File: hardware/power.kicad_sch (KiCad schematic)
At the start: 50 parts, among them J1 B2B-PH-K-S, J2 DX07S016JA1R1500, J3 PRPC001DAAN-RC, J4 PRPC001DAAN-RC, J5 PRPC001DAAN-RC, J6 PRPC001DAAN-RC, J7 PRPC001DAAN-RC, Q1 IRLML2246TRPBF, Q2 IRLML6344TRPBF, Q3 IRLML6344TRPBF, Q4 IRLML2246TRPBF, U1 USBLC6-2SC6, U2 S-8240ADQ-M6T1U, U3 BQ21040DBVR, U4 TPS63031DSK

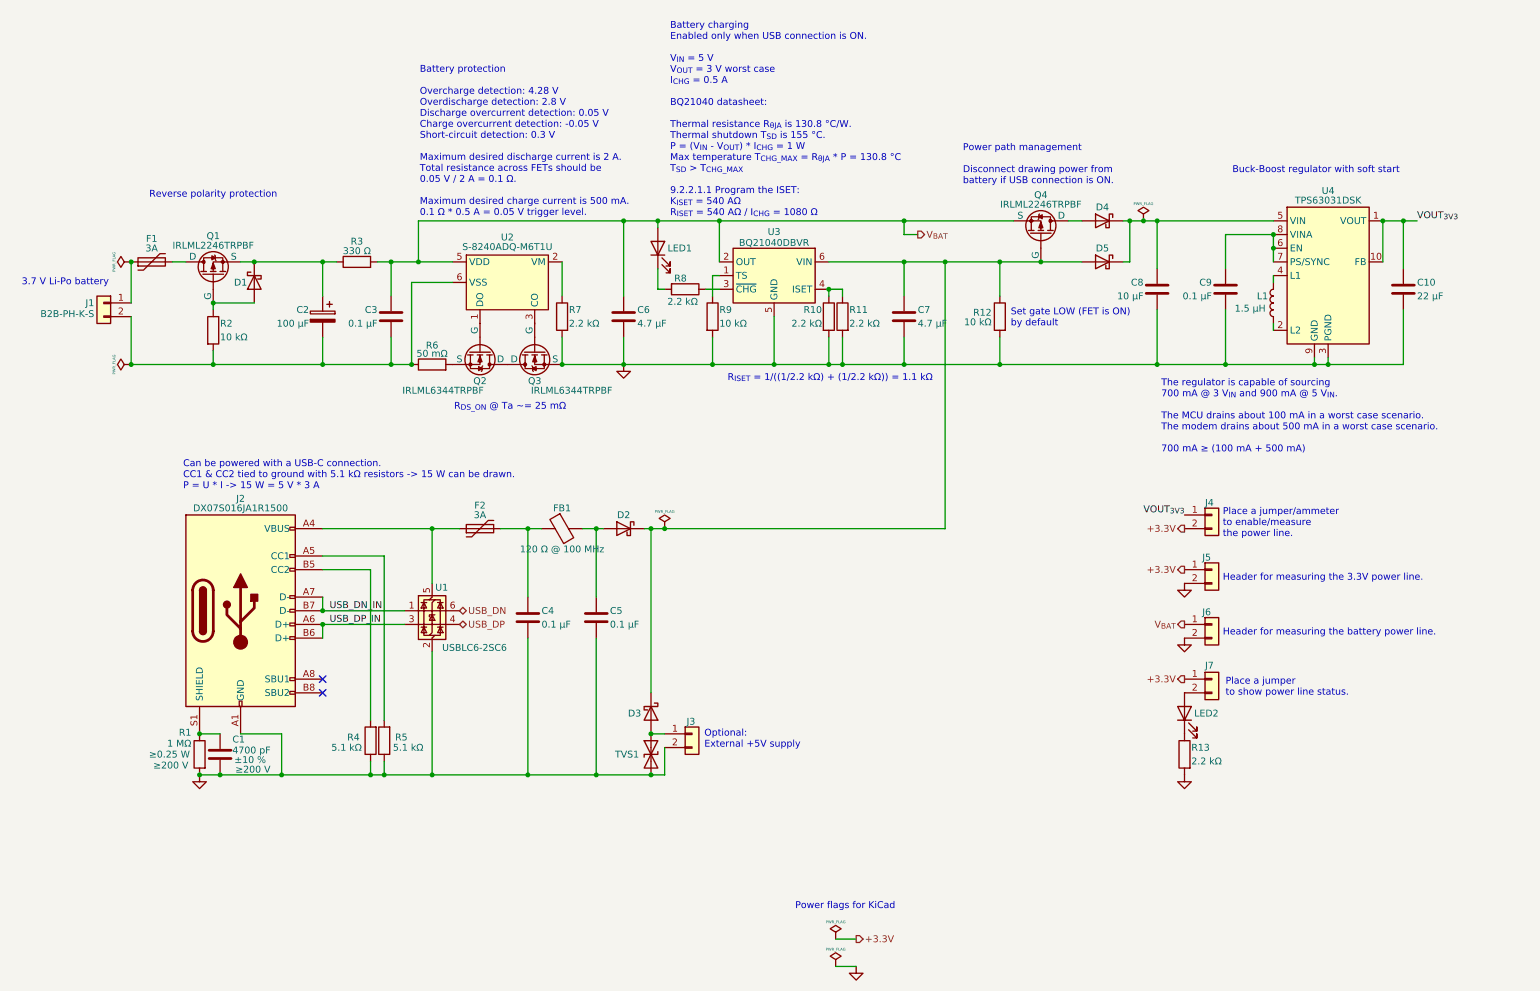
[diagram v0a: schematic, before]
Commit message: HW: Add battery sense, refine schema and components
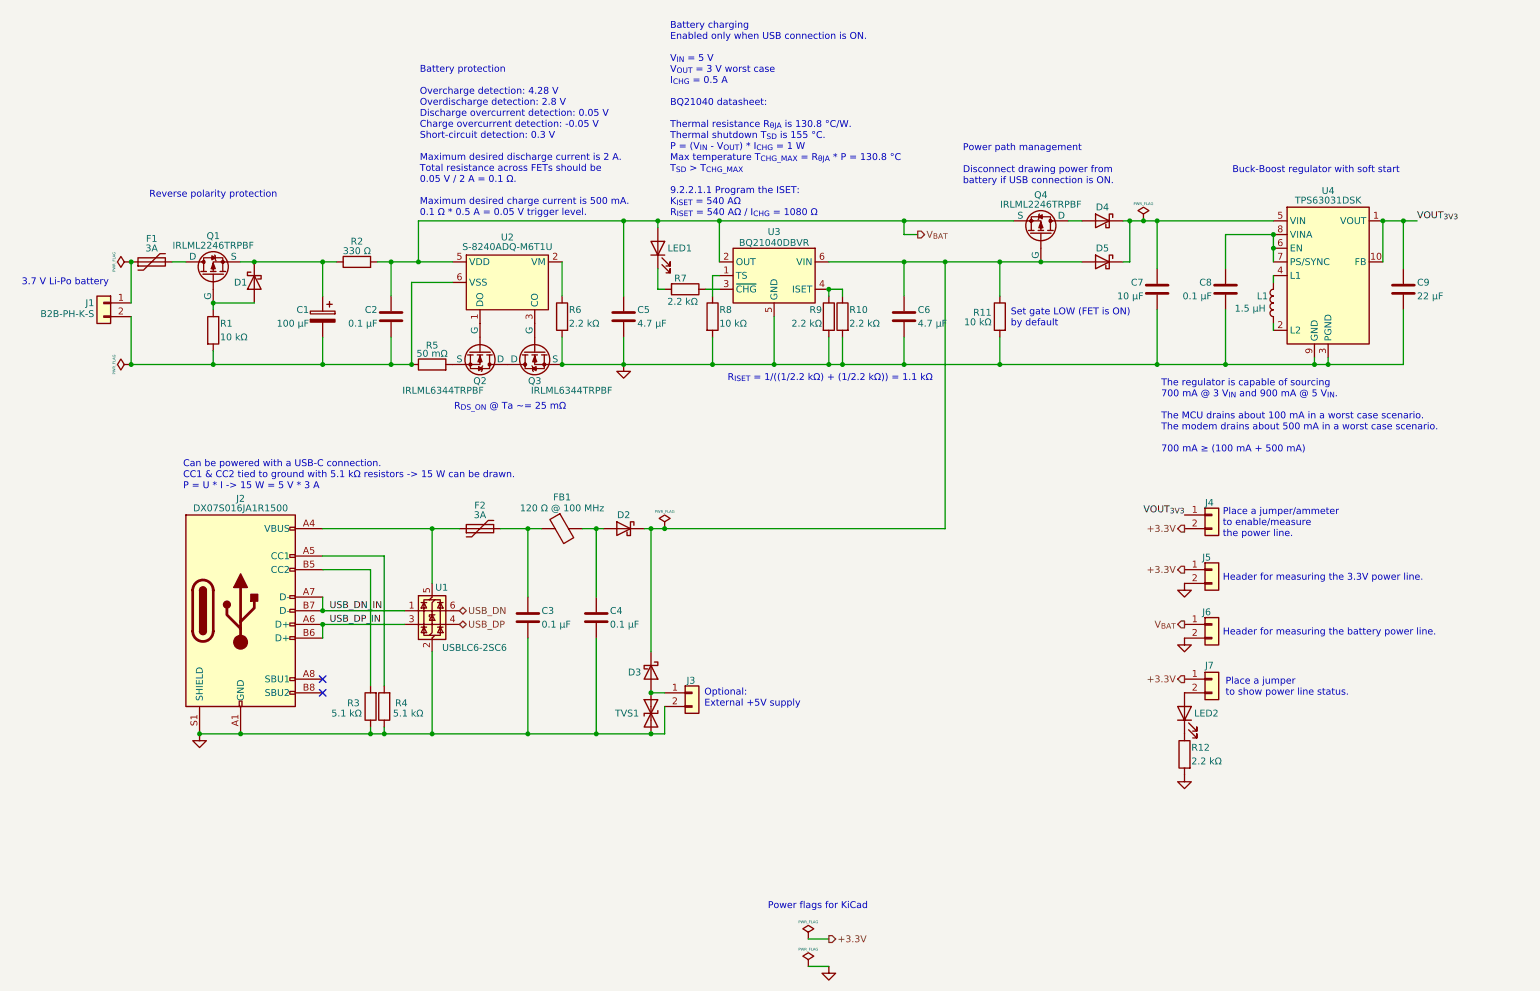
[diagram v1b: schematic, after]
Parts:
- removed C1: 4700 pF, Capacitor_SMD:C_0805_2012Metric_Pad1.18x1.45mm_HandSolder, symbol Device:C
- removed R1: 1 MΩ, Resistor_SMD:R_1206_3216Metric_Pad1.30x1.75mm_HandSolder, symbol Device:R
- C5: renamed from C6; footprint Capacitor_SMD:C_0805_2012Metric_Pad1.18x1.45mm_HandSolder -> Capacitor_SMD:C_0603_1608Metric_Pad1.08x0.95mm_HandSolder; Digi-Key Part Number 732-7623-1-ND -> 1276-1044-1-ND; Manufacturer Würth Elektronik -> Samsung Electro-Mechanics; Manufacturer Part Number 885012107013 -> CL10A475KP8NNNC
- C6: renamed from C7; footprint Capacitor_SMD:C_0805_2012Metric_Pad1.18x1.45mm_HandSolder -> Capacitor_SMD:C_0603_1608Metric_Pad1.08x0.95mm_HandSolder; Digi-Key Part Number 732-7623-1-ND -> 1276-1044-1-ND; Manufacturer Würth Elektronik -> Samsung Electro-Mechanics; Manufacturer Part Number 885012107013 -> CL10A475KP8NNNC
- C9: renamed from C10; footprint Capacitor_SMD:C_0805_2012Metric_Pad1.18x1.45mm_HandSolder -> Capacitor_SMD:C_0603_1608Metric_Pad1.08x0.95mm_HandSolder; Digi-Key Part Number 732-7616-1-ND -> 1276-1274-1-ND; Manufacturer Würth Elektronik -> Samsung Electro-Mechanics; Manufacturer Part Number 885012107005 -> CL10A226MP8NUNE
- R3: renamed from R4; footprint Resistor_SMD:R_0805_2012Metric_Pad1.20x1.40mm_HandSolder -> Resistor_SMD:R_0603_1608Metric_Pad0.98x0.95mm_HandSolder; Digi-Key Part Number 732-560112120019CT-ND -> 541-10481-1-ND; Manufacturer Würth Elektronik -> Vishay Dale; Manufacturer Part Number 560112120019 -> RCS06035K10FKEA
- R4: renamed from R5; footprint Resistor_SMD:R_0805_2012Metric_Pad1.20x1.40mm_HandSolder -> Resistor_SMD:R_0603_1608Metric_Pad0.98x0.95mm_HandSolder; Digi-Key Part Number 732-560112120019CT-ND -> 541-10481-1-ND; Manufacturer Würth Elektronik -> Vishay Dale; Manufacturer Part Number 560112120019 -> RCS06035K10FKEA
- renumbered C2 to C1, C3 to C2, C4 to C3, C5 to C4, C8 to C7, C9 to C8, R2 to R1, R11 to R10, R12 to R11, R13 to R12, R3 to R2, R6 to R5, R7 to R6, R8 to R7, R9 to R8, R10 to R9
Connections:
- net GND: now also J2.S1 (SHIELD)
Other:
- moved on the sheet: D3, J3, R3, R4, TVS1

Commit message: HW: Refactor
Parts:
- added C10: 10 µF, Capacitor_SMD:C_0603_1608Metric_Pad1.08x0.95mm_HandSolder, symbol Device:C
- C1, C2, C3, C4, C5, C6, C7, C8, D1, D2, D3, D4, D5, F1, F2, FB1, J1, J2, J3, J4, J5, J6, J7, L1, LED1, LED2, Q1, Q2, Q3, Q4, R1, R10, R11, R12, R2, R3, R4, R5, R6, R7, R8, R9, TVS1, U1, U2, U3, U4: Footprint review check (none) -> +
- C9: value 22 µF -> 10 µF; Digi-Key Part Number 1276-1274-1-ND -> 732-7903-1-ND; Footprint review check (none) -> +; Manufacturer Samsung Electro-Mechanics -> Würth Elektronik; Manufacturer Part Number CL10A226MP8NUNE -> 885012106006
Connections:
- net GND: now also C10.2
- net VOUT_{3V3}: now also C10.1
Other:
- moved on the sheet: C7, C8, L1, U4

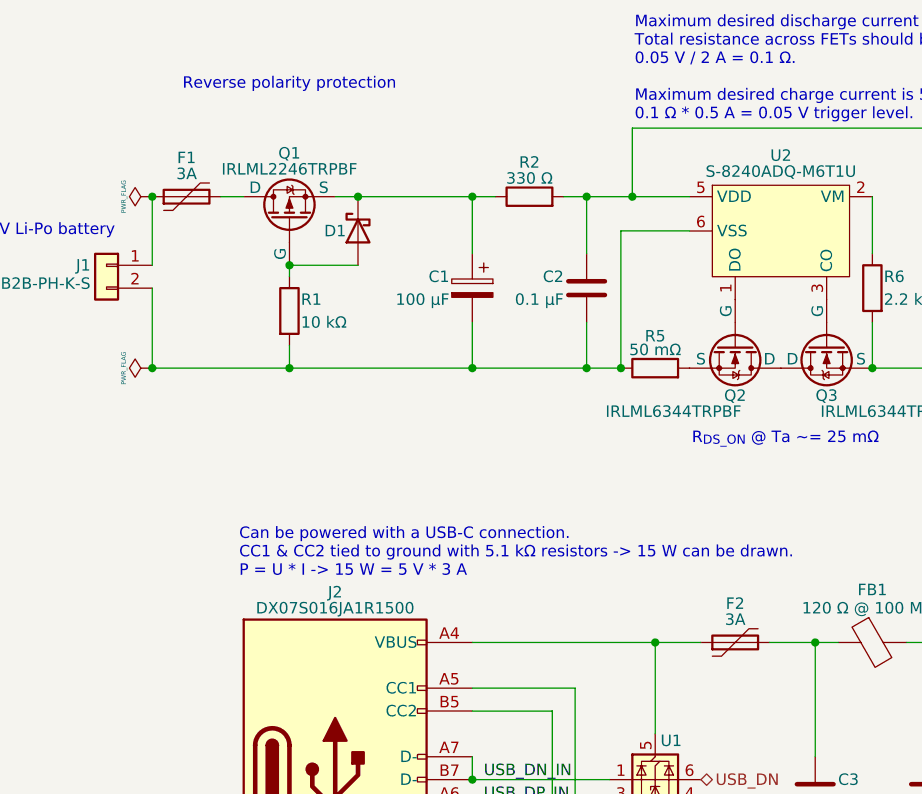
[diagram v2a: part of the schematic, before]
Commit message: HW: Fix fuses, refactor BOM for Aisler plugin
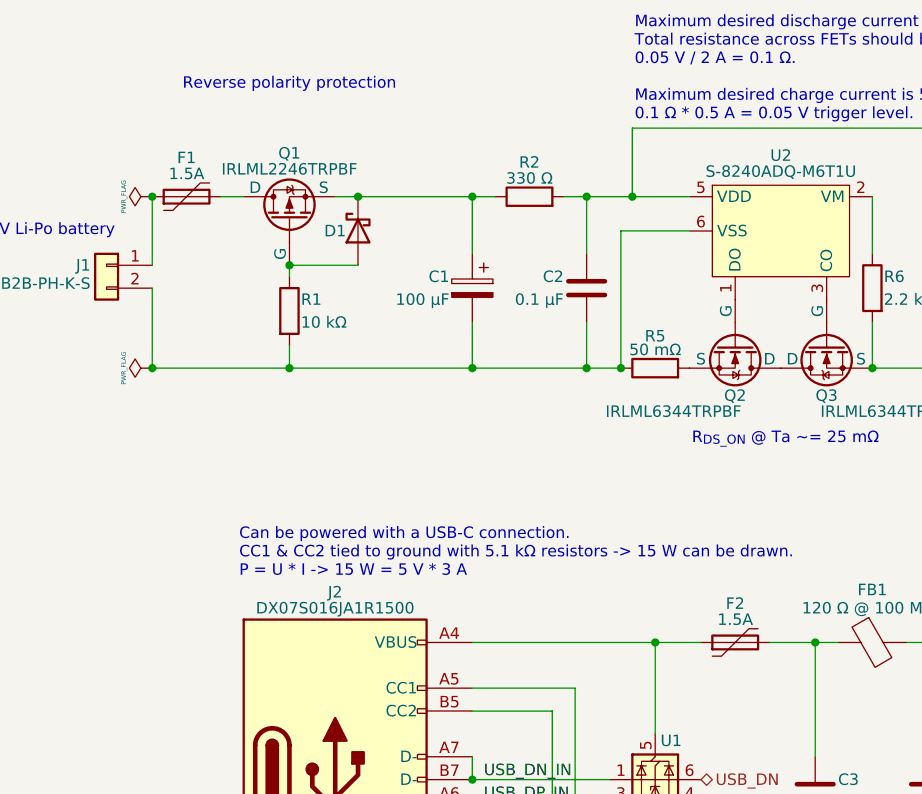
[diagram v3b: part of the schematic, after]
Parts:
- C1: MPN (none) -> 865080142007; Manufacturer Part Number 865080142007 -> (none)
- C10, C7, C9: MPN (none) -> 885012106006; Manufacturer Part Number 885012106006 -> (none)
- C2, C3, C4, C8: MPN (none) -> 885012206071; Manufacturer Part Number 885012206071 -> (none)
- C5, C6: MPN (none) -> CL10A475KP8NNNC; Manufacturer Part Number CL10A475KP8NNNC -> (none)
- D1, D2, D3, D4, D5: MPN (none) -> BAT60AE6327HTSA1; Manufacturer Part Number BAT60AE6327HTSA1 -> (none)
- F1, F2: value 3A -> 1.5A; MPN (none) -> PTSLR08056V150; Manufacturer Part Number PTSLR08056V150 -> (none)
- FB1: MPN (none) -> BLM18KG121TN1D; Manufacturer Part Number BLM18KG121TN1D -> (none)
- J1: MPN (none) -> B2B-PH-K-S; Manufacturer Part Number B2B-PH-K-S -> (none)
- J2: MPN (none) -> DX07S016JA1R1500; Manufacturer Part Number DX07S016JA1R1500 -> (none)
- J3, J4, J5, J6, J7: MPN (none) -> PRPC001DAAN-RC; Manufacturer Part Number PRPC001DAAN-RC -> (none)
- L1: MPN (none) -> NR3015T1R5N; Manufacturer Part Number NR3015T1R5N -> (none)
- LED1, LED2: MPN (none) -> 150141YS73100; Manufacturer Part Number 150141YS73100 -> (none)
- Q1, Q4: MPN (none) -> IRLML2246TRPBF; Manufacturer Part Number IRLML2246TRPBF -> (none)
- Q2, Q3: MPN (none) -> IRLML6344TRPBF; Manufacturer Part Number IRLML6344TRPBF -> (none)
- R1, R11, R8: MPN (none) -> 560112116005; Manufacturer Part Number 560112116005 -> (none)
- R10, R12, R6, R7, R9: MPN (none) -> 560112116098; Manufacturer Part Number 560112116098 -> (none)
- R2: MPN (none) -> 560112116020; Manufacturer Part Number 560112116020 -> (none)
- R3, R4: MPN (none) -> RCS06035K10FKEA; Manufacturer Part Number RCS06035K10FKEA -> (none)
- R5: MPN (none) -> ERJ-3BWFR050V; Manufacturer Part Number ERJ-3BWFR050V -> (none)
- TVS1: MPN (none) -> SMAJ6.0CA; Manufacturer Part Number SMAJ6.0CA -> (none)
- U1: MPN (none) -> USBLC6-2SC6; Manufacturer Part Number USBLC6-2SC6 -> (none)
- U2: MPN (none) -> S-8240ADQ-M6T1U; Manufacturer Part Number S-8240ADQ-M6T1U -> (none)
- U3: MPN (none) -> BQ21040DBVR; Manufacturer Part Number BQ21040DBVR -> (none)
- U4: MPN (none) -> TPS63031DSKR; Manufacturer Part Number TPS63031DSKR -> (none)

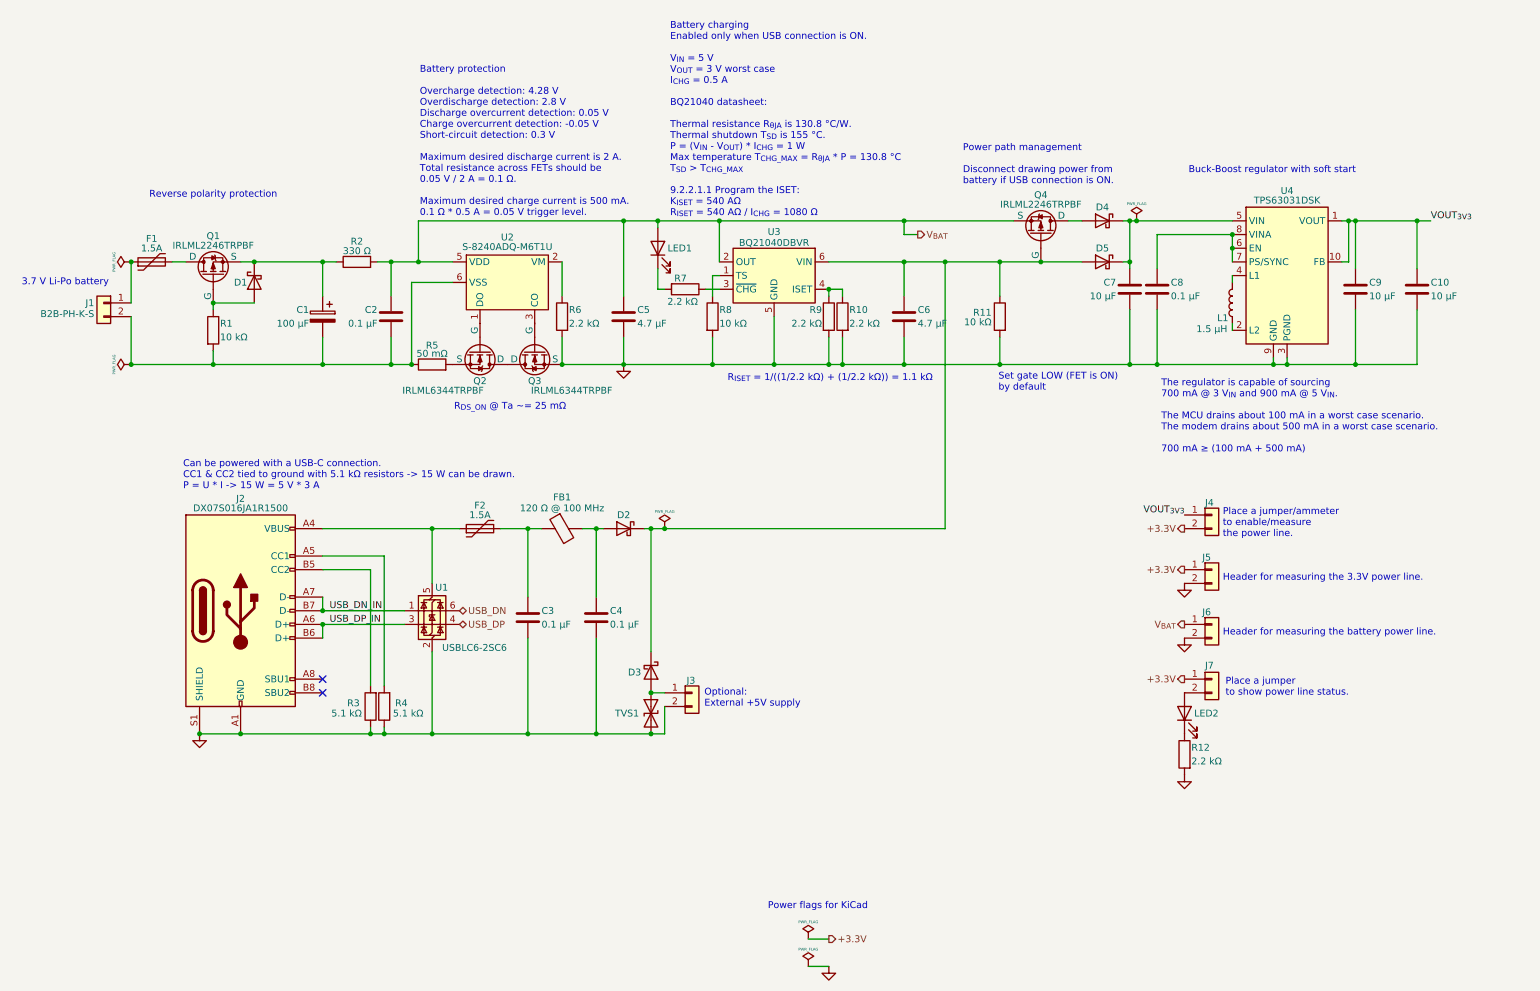
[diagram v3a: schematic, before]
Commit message: HW: Refactor power section
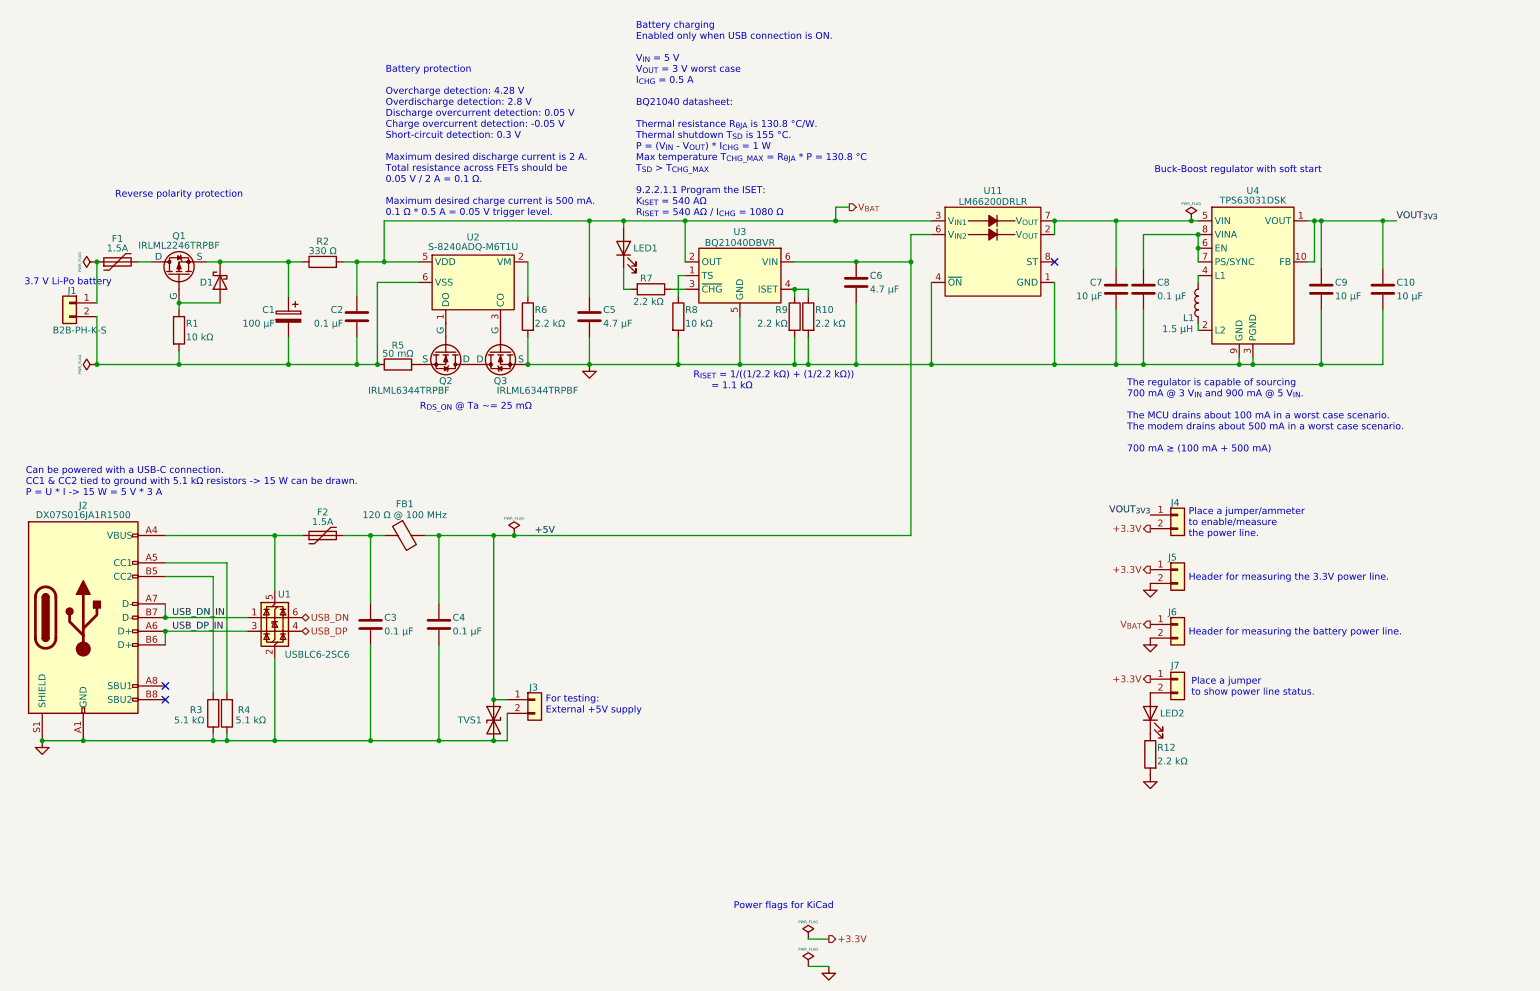
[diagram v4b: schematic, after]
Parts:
- removed D2, D3, D4, D5: BAT60AE6327HTSA1, Diode_SMD:D_SOD-323_HandSoldering, symbol Device:D_Schottky
- removed Q4: IRLML2246TRPBF, Package_TO_SOT_SMD:SC-59_Handsoldering, symbol IRLML2246TRPBF:IRLML2246TRPBF
- removed R11: 10 kΩ, Resistor_SMD:R_0603_1608Metric_Pad0.98x0.95mm_HandSolder, symbol Device:R
- added U11: LM66200DRLR, Package_TO_SOT_SMD:SOT-583-8, symbol LM66200:LM66200
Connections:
- net GND: now also U11.1 (GND), U11.4 (~{ON}), U11.5 (GND)
- net V_{BAT}: now also U11.3 (V_{IN1})
- net +5V: now reaches C6.1, U3.6 (VIN)
- net +5V: now also C4.1, FB1.2, J3.1 (Pin_1), TVS1.1 (A1), U11.6 (V_{IN2})
- net at C7.1, U4.5 (VIN): now also U11.2 (V_{OUT}), U11.7 (V_{OUT})
- no-connect marks 2 -> 3
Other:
- note added: "For testing: External +5V supply"
- note removed: "Optional: External +5V supply"
- note removed: "Power path management Disconnect drawing power from battery if USB connection is ON."
- note removed: "Set gate LOW (FET is ON) by default"
- moved on the sheet: C1, C10, C2, C3, C4, C5, C6, C7, C8, C9, D1, F1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

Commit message: HW: Rework layout
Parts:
- D1: value BAT60AE6327HTSA1 -> BAT60A
- renumbered R12 to R11, R3 to R2, R4 to R3, R2 to R4, U11 to U4, U4 to U5
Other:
- moved on the sheet: C1, C10, C2, C3, C4, C5, C6, C7, C8, C9, D1, F1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
